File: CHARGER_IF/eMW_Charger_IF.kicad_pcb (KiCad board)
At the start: 2 copper layers, 67 x 129 mm, 13 parts, among them J1 CONN_01X02, J2 Booster_J1_J3, J3 Booster_J4_J2, U1 V7805-2000R, U2 ArduinoSocket, U3 SN74ACT08N, U4 SN74ACT08N

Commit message: Charger IF WIP
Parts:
- added J4: CONN_02X10, Pin_Headers:Pin_Header_Straight_2x10_Pitch2.54mm, F.Cu at (246.8, 66.0)
- added J5: CONN_02X10, Pin_Headers:Pin_Header_Straight_2x10_Pitch2.54mm, F.Cu at (122.8, 45.5)
- U2: value ArduinoSocket -> Arduino-Socket; footprint Pin_Headers:Pin_Header_Straight_2x10_Pitch2.54mm -> eMW_Charger:eMW-Control-Board-Arduino-Header
- moved U2 127.5 mm to (240.2, 92.5), turned to 0 degrees
- moved C2 39.6 mm to (156.2, 93.0), turned to 270 degrees
- moved U1 26.5 mm to (138.0, 95.2), turned to 180 degrees
- moved U3 17.1 mm to (136.8, 39.8)
- moved U4 14.8 mm to (144.5, 80.5)
- moved C1 14.2 mm to (156.2, 105.2)
- moved J1 8.81 mm to (133.2, 107.5), turned to 90 degrees
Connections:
- J2 pad 1: Net-(J2-Pad1) -> (no net)
- J2 pad 10: Net-(J2-Pad10) -> (no net)
- J2 pad 29: Net-(J2-Pad29) -> (no net)
- J2 pad 30: Net-(J2-Pad30) -> (no net)
- J2 pad 7: Net-(J2-Pad7) -> (no net)
- J2 pad 8: Net-(J2-Pad8) -> (no net)
- J2 pad 9: Net-(J2-Pad9) -> (no net)
- J3 pad 11: Net-(J3-Pad11) -> (no net)
- J3 pad 12: Net-(J3-Pad12) -> (no net)
- J3 pad 13: Net-(J3-Pad13) -> (no net)
- J3 pad 14: Net-(J3-Pad14) -> (no net)
- J3 pad 15: Net-(J3-Pad15) -> (no net)
- J3 pad 16: Net-(J3-Pad16) -> (no net)
- J3 pad 17: Net-(J3-Pad17) -> (no net)
- J3 pad 18: Net-(J3-Pad18) -> (no net)
- J3 pad 19: Net-(J3-Pad19) -> (no net)
- J3 pad 20: Net-(J3-Pad20) -> (no net)
- J3 pad 31: Net-(J3-Pad31) -> (no net)
- J3 pad 32: Net-(J3-Pad32) -> (no net)
- R1 pad 1: Net-(R1-Pad1) -> Net-(J5-Pad6)
- R3 pad 1: Net-(R3-Pad1) -> Net-(J5-Pad3)
- U2 pad 12: Net-(U2-Pad12) -> Net-(J4-Pad12)
- U2 pad 13: Net-(U2-Pad13) -> Net-(J4-Pad9)
- U2 pad 14: Net-(U2-Pad14) -> Net-(J4-Pad10)
- U2 pad 15: Net-(U2-Pad15) -> (no net)
- U2 pad 16: Net-(U2-Pad16) -> Net-(J4-Pad7)
- U2 pad 17: Net-(U2-Pad17) -> Net-(J4-Pad8)
- U2 pad 18: Net-(U2-Pad18) -> Net-(J4-Pad5)
- U2 pad 19: Net-(R1-Pad1) -> Net-(J4-Pad6)
- U2 pad 2: GND -> (no net)
- U2 pad 20: Net-(R3-Pad1) -> Net-(J4-Pad3)
- U2 pad 4: Net-(U2-Pad4) -> (no net)
- U2 pad 5: Net-(J2-Pad24) -> Net-(J4-Pad14)
- U2 pad 6: (no net) -> Net-(J4-Pad16)
- U2 pad 7: Net-(J2-Pad2) -> Net-(J4-Pad17)
- U2 pad 8: Net-(J2-Pad6) -> Net-(J4-Pad18)
- U3 pad 11: Net-(U2-Pad16) -> Net-(J5-Pad8)
- U3 pad 3: Net-(U2-Pad18) -> Net-(J5-Pad4)
- U3 pad 6: Net-(U2-Pad17) -> Net-(J5-Pad5)
- U3 pad 8: Net-(U2-Pad14) -> Net-(J5-Pad7)
- U4 pad 11: Net-(U4-Pad11) -> (no net)
- U4 pad 3: Net-(U2-Pad13) -> Net-(J5-Pad10)
- U4 pad 6: Net-(U2-Pad12) -> Net-(J5-Pad9)
- U4 pad 8: Net-(U4-Pad8) -> (no net)
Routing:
- net Net-(J4-Pad12): track 0.00 -> 31.0 mm
- net Net-(J2-Pad4): track 0.00 -> 29.7 mm
- net Net-(J2-Pad3): track 0.00 -> 22.9 mm
- net Net-(J4-Pad10): track 0.00 -> 19.3 mm
- net Net-(J4-Pad9): track 0.00 -> 17.2 mm
- net Net-(J4-Pad8): track 0.00 -> 14.5 mm
- net Net-(J4-Pad17): track 0.00 -> 13.7 mm
- net Net-(J4-Pad14): track 0.00 -> 13.4 mm
- net Net-(J4-Pad13): track 0.00 -> 13.2 mm
- net Net-(J4-Pad15): track 0.00 -> 13.1 mm
- net Net-(J4-Pad7): track 0.00 -> 12.2 mm
- net Net-(J4-Pad6): track 0.00 -> 11.7 mm
- net Net-(J4-Pad16): track 0.00 -> 10.9 mm
- net Net-(J4-Pad19): track 0.00 -> 10.3 mm
- net Net-(J4-Pad18): track 0.00 -> 10.2 mm
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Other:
- board size 67 x 129 mm -> 18 x 33 mm

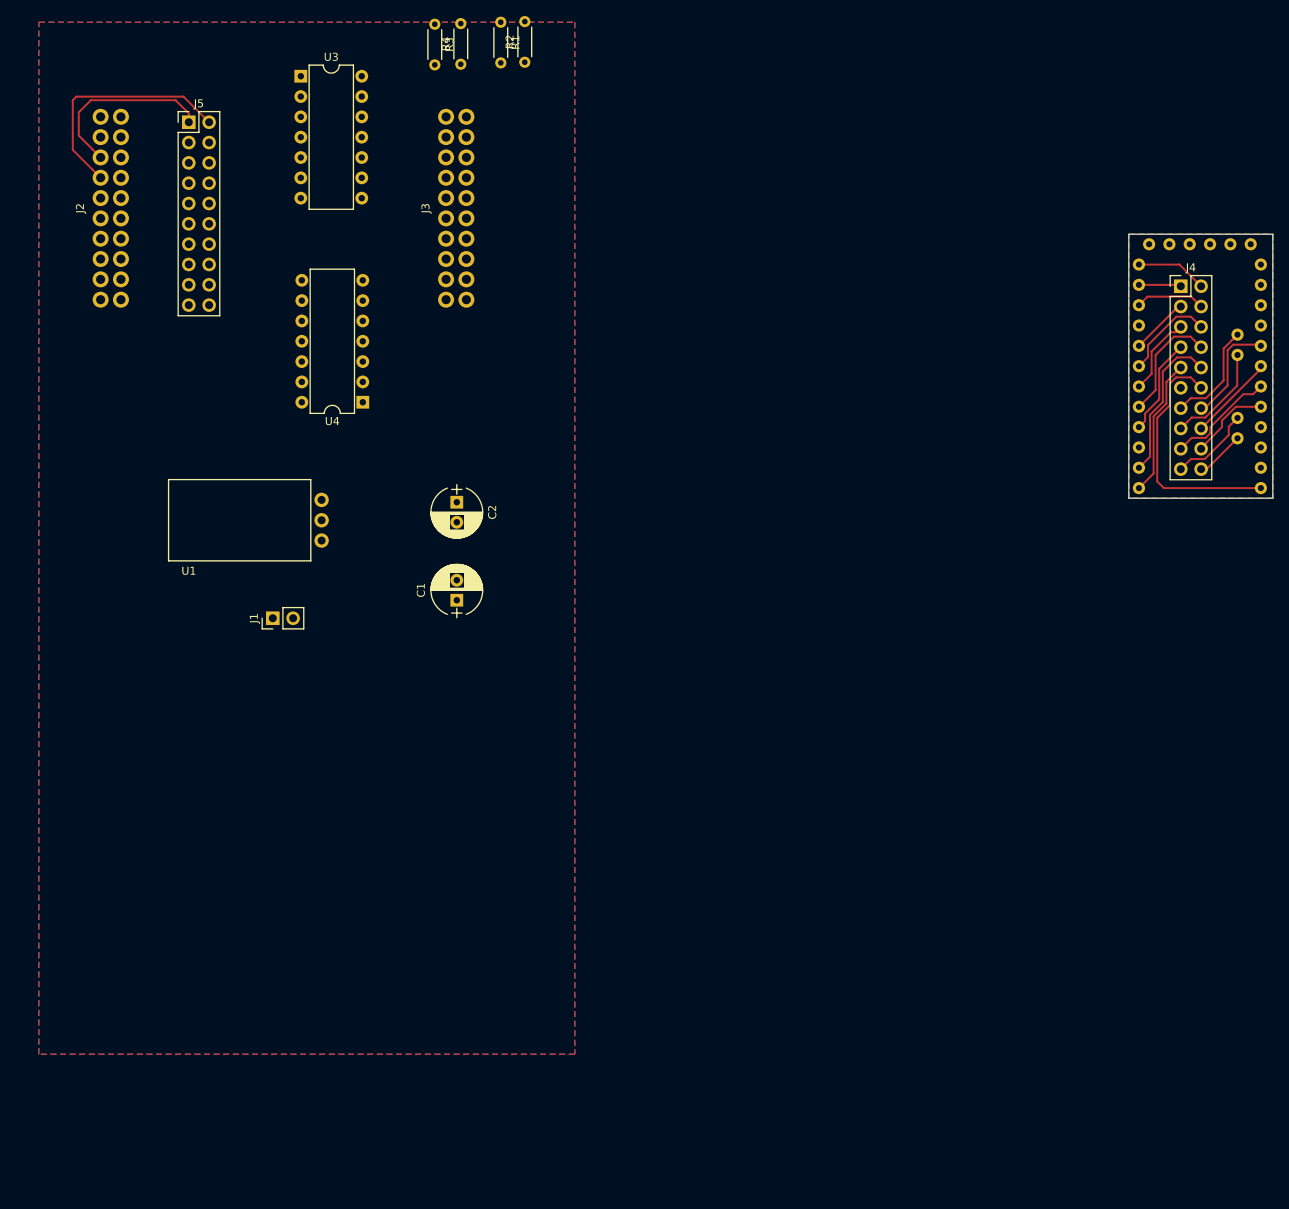
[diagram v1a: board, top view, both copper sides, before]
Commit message: Charger IF WIP
Mostly just need to double check all the mechanics and add a few
mounting holes
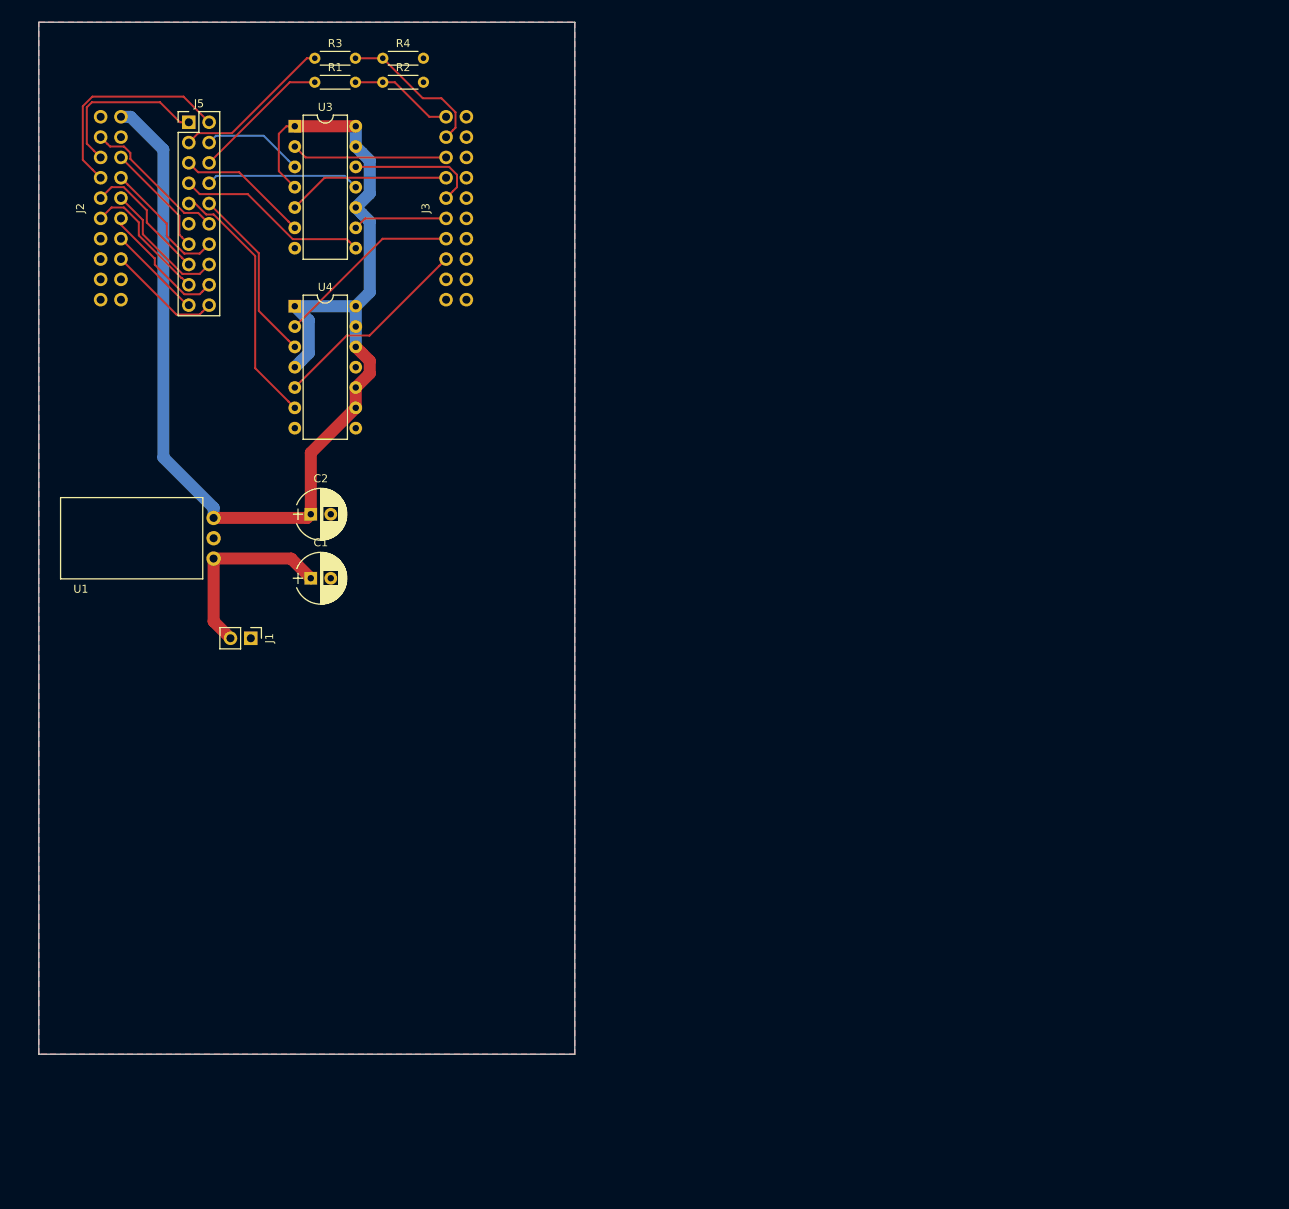
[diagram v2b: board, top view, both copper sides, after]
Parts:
- removed J4: CONN_02X10, Pin_Headers:Pin_Header_Straight_2x10_Pitch2.54mm
- removed U2: Arduino-Socket, eMW_Charger:eMW-Control-Board-Arduino-Header
- moved R1 24.4 mm to (138.5, 40.5), turned to 0 degrees
- moved C1 18.5 mm to (138.0, 102.5), turned to 0 degrees
- moved C2 18.3 mm to (138.0, 94.5), turned to 0 degrees
- moved R2 17.9 mm to (147.0, 40.5), turned to 0 degrees
- moved R3 15.6 mm to (138.5, 37.5), turned to 0 degrees
- moved U4 14.7 mm to (136.0, 68.5), turned to 0 degrees
- moved U1 13.7 mm to (124.5, 97.5)
- moved R4 9.78 mm to (147.0, 37.5), turned to 0 degrees
- moved U3 6.29 mm to (136.0, 46.0)
- moved J1 3.72 mm to (130.5, 110.0), turned to 270 degrees
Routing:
- net +5V: track 0.00 -> 157.4 mm
- net Net-(J5-Pad9): track 0.00 -> 32.0 mm
- net Net-(J4-Pad12): track 31.0 -> 0.00 mm
- net Net-(J3-Pad33): track 0.00 -> 25.6 mm
- net Net-(J5-Pad7): track 0.00 -> 24.2 mm
- net +12V: track 0.00 -> 24.0 mm
- net Net-(J3-Pad34): track 0.00 -> 23.5 mm
- net Net-(J5-Pad10): track 0.00 -> 22.4 mm
- net Net-(J3-Pad37): track 0.00 -> 20.5 mm
- net Net-(J5-Pad3): track 0.00 -> 20.1 mm
- net Net-(J3-Pad38): track 0.00 -> 19.5 mm
- net Net-(J4-Pad10): track 19.3 -> 0.00 mm
- net Net-(J5-Pad8): track 0.00 -> 19.3 mm
- net Net-(J3-Pad39): track 0.00 -> 18.9 mm
- net Net-(J2-Pad2): track 0.00 -> 18.5 mm
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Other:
- board size 18 x 33 mm -> 67 x 129 mm

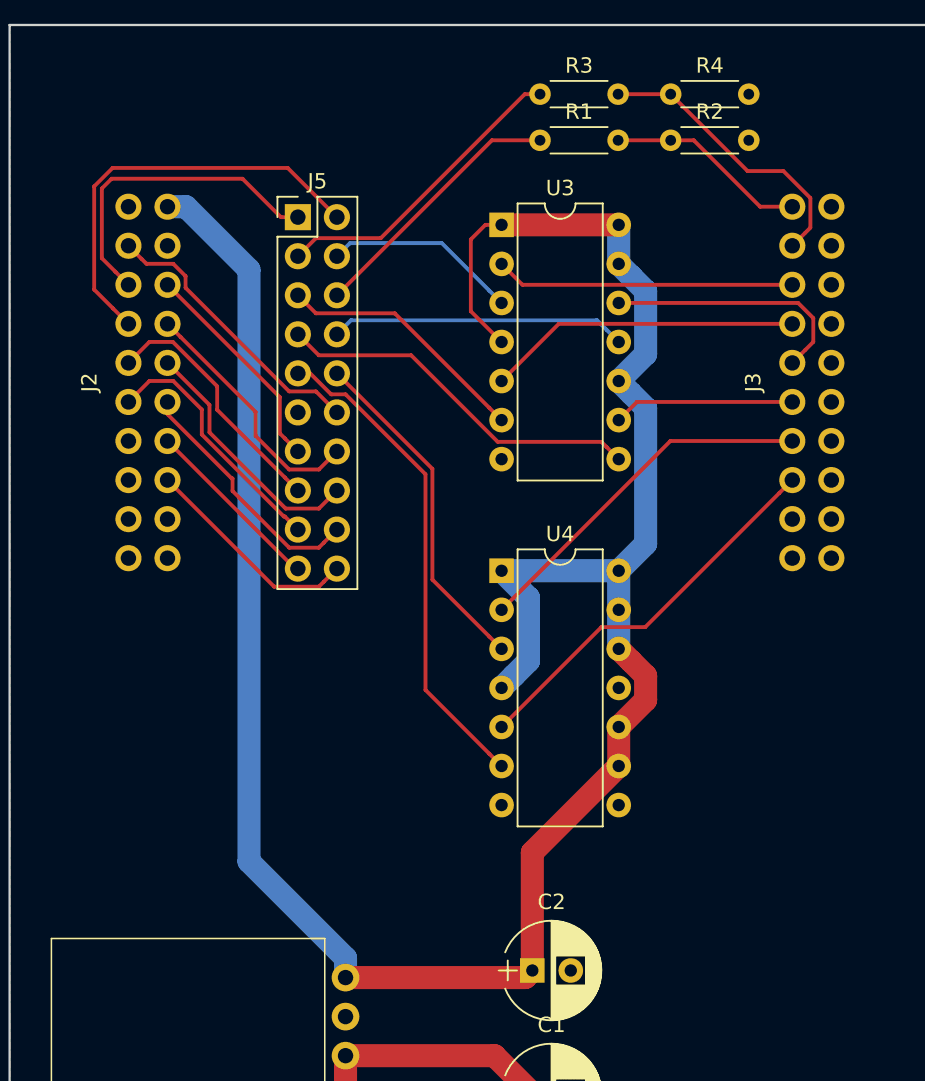
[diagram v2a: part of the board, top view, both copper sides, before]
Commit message: updated to osh park design rules
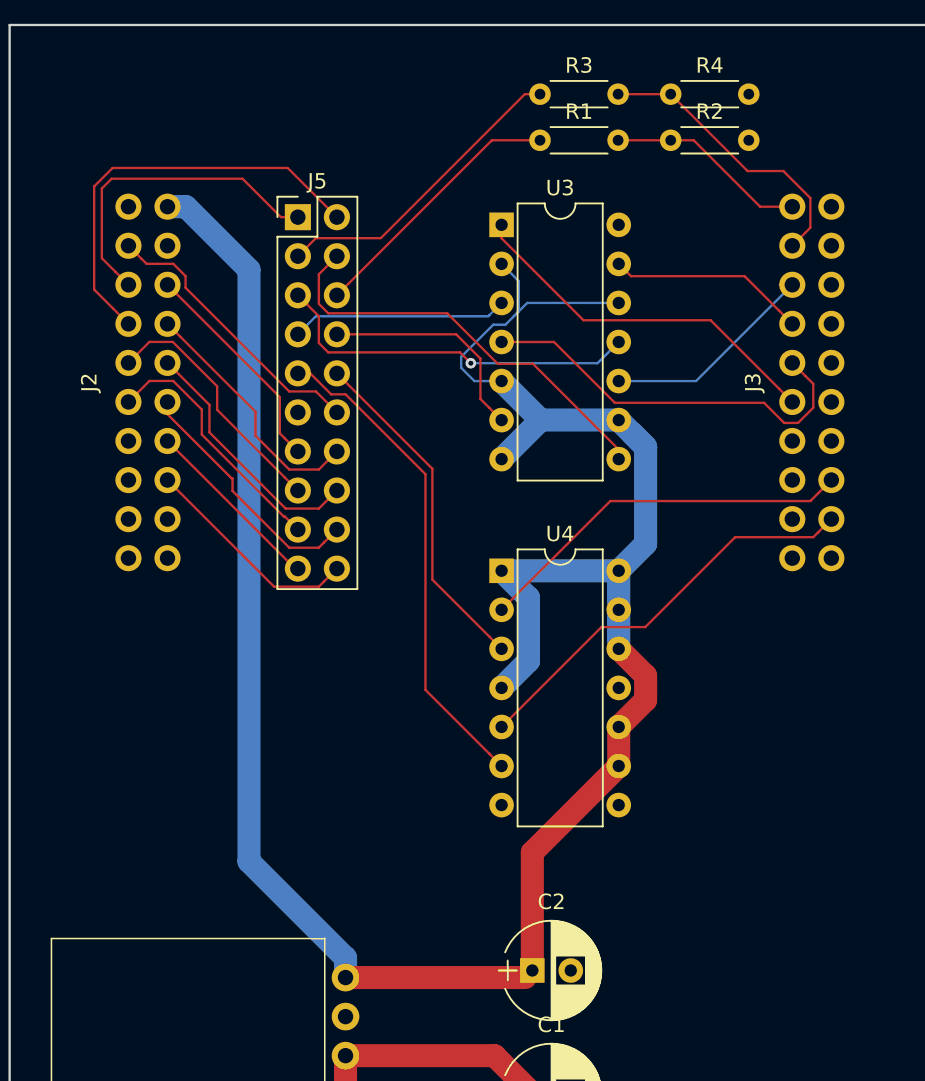
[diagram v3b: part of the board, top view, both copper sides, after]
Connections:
- J2 pad 1: (no net) -> Net-(J2-Pad1)
- J2 pad 10: (no net) -> Net-(J2-Pad10)
- J2 pad 29: (no net) -> Net-(J2-Pad29)
- J2 pad 30: (no net) -> Net-(J2-Pad30)
- J2 pad 7: (no net) -> Net-(J2-Pad7)
- J2 pad 8: (no net) -> Net-(J2-Pad8)
- J2 pad 9: (no net) -> Net-(J2-Pad9)
- J3 pad 11: (no net) -> Net-(J3-Pad11)
- J3 pad 12: (no net) -> Net-(J3-Pad12)
- J3 pad 13: (no net) -> Net-(J3-Pad13)
- J3 pad 14: (no net) -> Net-(J3-Pad14)
- J3 pad 15: (no net) -> Net-(J3-Pad15)
- J3 pad 16: (no net) -> Net-(J3-Pad16)
- J3 pad 17: (no net) -> Net-(J3-Pad17)
- J3 pad 18: (no net) -> Net-(J3-Pad18)
- J3 pad 19: (no net) -> Net-(J3-Pad19)
- J3 pad 20: (no net) -> Net-(J3-Pad20)
- J3 pad 31: (no net) -> Net-(J3-Pad31)
- J3 pad 32: (no net) -> Net-(J3-Pad32)
- U3 pad 1: +5V -> Net-(J3-Pad35)
- U3 pad 10: +5V -> Net-(J3-Pad38)
- U3 pad 11: Net-(J5-Pad8) -> Net-(J5-Pad5)
- U3 pad 12: Net-(J3-Pad36) -> +5V
- U3 pad 13: +5V -> Net-(J3-Pad37)
- U3 pad 14: +5V -> GND
- U3 pad 2: Net-(J3-Pad38) -> +5V
- U3 pad 3: Net-(J5-Pad4) -> Net-(J5-Pad7)
- U3 pad 4: +5V -> Net-(J3-Pad36)
- U3 pad 5: Net-(J3-Pad37) -> +5V
- U3 pad 6: Net-(J5-Pad5) -> Net-(J5-Pad8)
- U3 pad 7: GND -> +5V
- U3 pad 8: Net-(J5-Pad7) -> Net-(J5-Pad4)
- U3 pad 9: Net-(J3-Pad35) -> +5V
- U4 pad 11: (no net) -> Net-(U4-Pad11)
- U4 pad 2: Net-(J3-Pad34) -> Net-(J3-Pad13)
- U4 pad 5: Net-(J3-Pad33) -> Net-(J3-Pad12)
- U4 pad 8: (no net) -> Net-(U4-Pad8)
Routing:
- net Net-(J3-Pad12): track 0.00 -> 27.1 mm
- net Net-(J3-Pad33): track 25.6 -> 0.00 mm
- net Net-(J3-Pad13): track 0.00 -> 24.9 mm
- net Net-(J3-Pad34): track 23.5 -> 0.00 mm
- net Net-(J5-Pad4): track 12.7 -> 27.6 mm
- net Net-(J3-Pad35): track 11.8 -> 24.2 mm
- net Net-(J5-Pad7): track 24.2 -> 14.1 mm
- net Net-(J3-Pad36): track 16.5 -> 26.3 mm
- net Net-(J5-Pad5): track 16.6 -> 24.3 mm, vias 0 -> 1
- net Net-(J3-Pad37): track 20.5 -> 12.9 mm
- net Net-(J3-Pad38): track 19.5 -> 14.7 mm
- net Net-(J5-Pad8): track 19.3 -> 14.6 mm
- net +5V: track 157.4 -> 160.0 mm
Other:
- net class Default: clearance 0.2 -> 0.1524; trace_width 0.25 -> 0.1524; via_dia 0.6 -> 0.6858; via_drill 0.4 -> 0.3302
- rule trace_clearance: 0.2 -> 0.1524
- rule trace_min: 0.2 -> 0.1524
- rule via_min_drill: 0.3 -> 0.3302
- rule via_min_size: 0.4 -> 0.6858
